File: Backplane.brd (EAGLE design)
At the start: 160 x 84 mm, 2 parts, among them X1 FAC64S

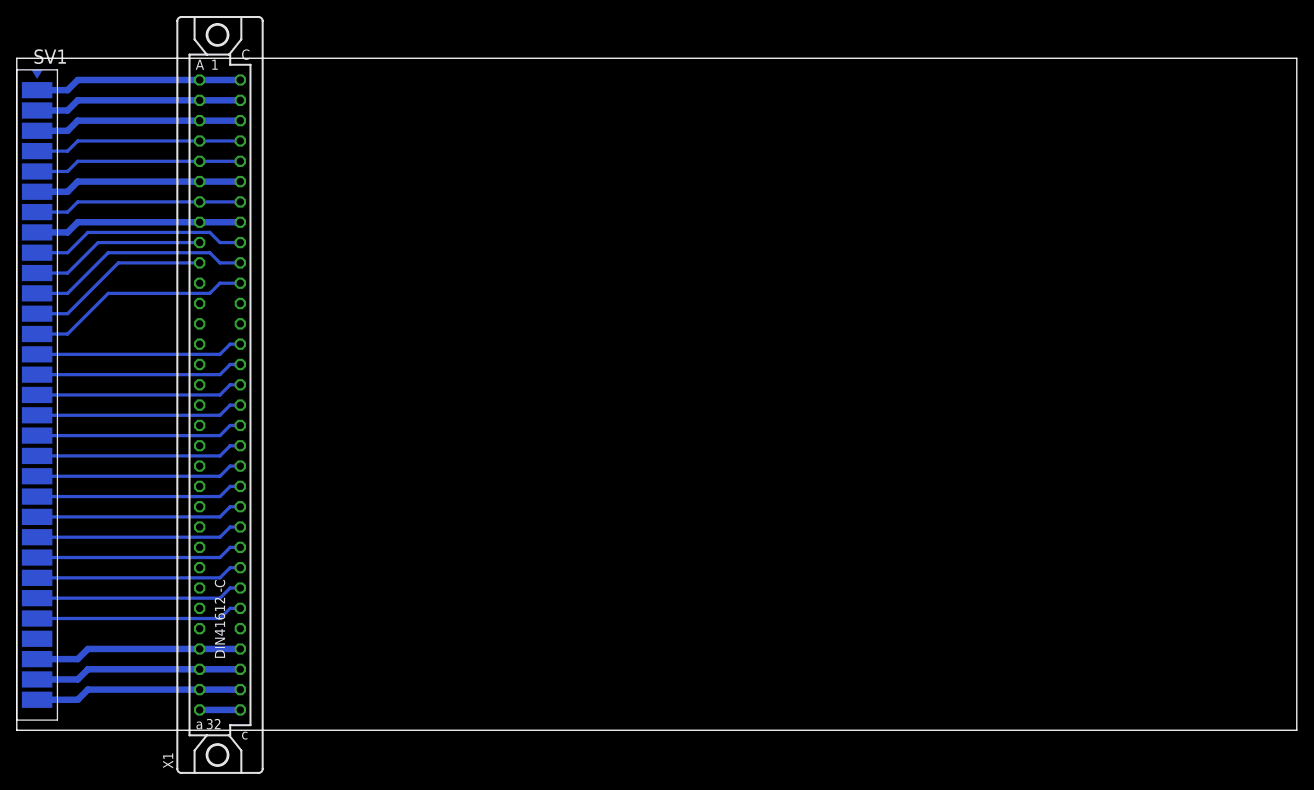
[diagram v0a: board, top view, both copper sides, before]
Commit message: Pi-Display hinzugefügt, Boards angepasst
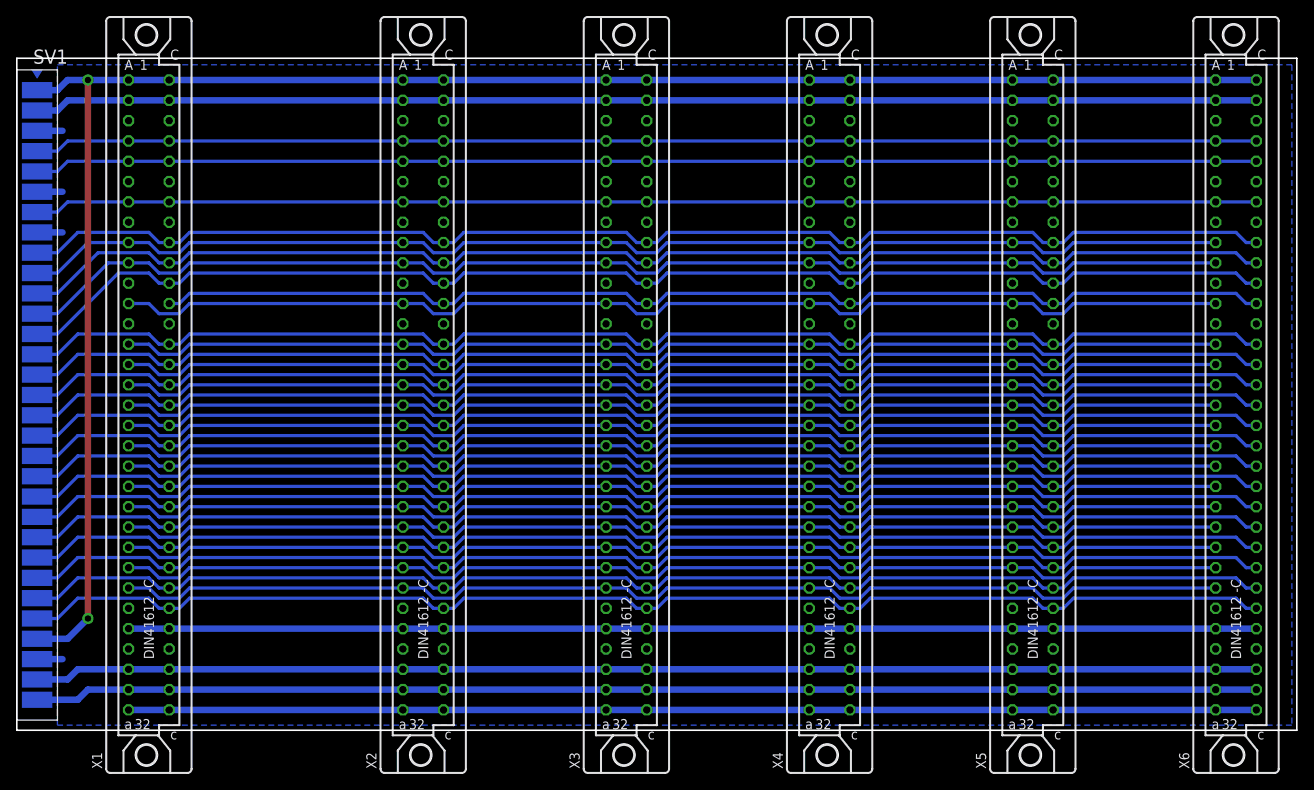
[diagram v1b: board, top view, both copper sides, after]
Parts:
- added X2, X3, X4, X5, X6: FAC64S, con-vg:FAC64S
- moved X1 8.89 mm to (16.5, 41.9)
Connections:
- new net A14: X1.A14, X2.A14, X3.A14, X4.A14, X5.A14, X6.A14
- new net A15: X1.A15, X2.A15, X3.A15, X4.A15, X5.A15, X6.A15
- new net A16: X1.A16, X2.A16, X3.A16, X4.A16, X5.A16, X6.A16
- new net A17: X1.A17, X2.A17, X3.A17, X4.A17, X5.A17, X6.A17
- new net A18: X1.A18, X2.A18, X3.A18, X4.A18, X5.A18, X6.A18
- new net A19: X1.A19, X2.A19, X3.A19, X4.A19, X5.A19, X6.A19
- new net A20: X1.A20, X2.A20, X3.A20, X4.A20, X5.A20, X6.A20
- new net A21: X1.A21, X2.A21, X3.A21, X4.A21, X5.A21, X6.A21
- new net A22: X1.A22, X2.A22, X3.A22, X4.A22, X5.A22, X6.A22
- new net A23: X1.A23, X2.A23, X3.A23, X4.A23, X5.A23, X6.A23
- new net A24: X1.A24, X2.A24, X3.A24, X4.A24, X5.A24, X6.A24
- new net A26: X1.A25, X2.A25, X3.A25, X4.A25, X5.A25, X6.A25
- net !PI_RESET: now also X2.A26, X3.A26, X4.A26, X5.A26, X6.A26
- net +24V: now also X2.A32, X2.C32, X3.A32, X3.C32, X4.A32, X4.C32, X5.A32, X5.C32, X6.A32, X6.C32
- net +3,3V: now also X2.A2, X2.C2, X3.A2, X3.C2, X4.A2, X4.C2, X5.A2, X5.C2, X6.A2, X6.C2
- net +5V_EXT: now also X2.A31, X2.C31, X3.A31, X3.C31, X4.A31, X4.C31, X5.A31, X5.C31, X6.A31, X6.C31
- net +5V_INT: now also X2.A1, X2.C1, X3.A1, X3.C1, X4.A1, X4.C1, X5.A1, X5.C1, X6.A1, X6.C1
- net +5V_INT2: now also X2.A28, X2.C28, X3.A28, X3.C28, X4.A28, X4.C28, X5.A28, X5.C28, X6.A28, X6.C28
- net 1WIRE: now also X2.A7, X2.C7, X3.A7, X3.C7, X4.A7, X4.C7, X5.A7, X5.C7, X6.A7, X6.C7
- net GND: now also X1.A11, X1.A13, X1.A27, X1.C13, X2.A11, X2.A13, X2.A27, X2.A29, X2.A3, X2.A6, X2.A8, X2.C13, X2.C29, X2.C3, X2.C6, X2.C8, X3.A11, X3.A13, X3.A27, X3.A29, X3.A3, X3.A6, X3.A8, X3.C13, X3.C29, X3.C3, X3.C6, X3.C8, X4.A11, X4.A13, X4.A27, X4.A29, X4.A3, X4.A6, X4.A8, X4.C13, X4.C29, X4.C3, X4.C6, X4.C8, X5.A11, X5.A13, X5.A27, X5.A29, X5.A3, X5.A6, X5.A8, X5.C13, X5.C29, X5.C3, X5.C6, X5.C8, X6.A11, X6.A13, X6.A27, X6.A29, X6.A3, X6.A6, X6.A8, X6.C13, X6.C29, X6.C3, X6.C6, X6.C8
- net GND_EXT: now also X2.A30, X2.C30, X3.A30, X3.C30, X4.A30, X4.C30, X5.A30, X5.C30, X6.A30, X6.C30
- net GPIO.05: now also X2.C14, X3.C14, X4.C14, X5.C14, X6.C14
- net GPIO.06: now also X2.C15, X3.C15, X4.C15, X5.C15, X6.C15
- net GPIO.12: now also X2.C16, X3.C16, X4.C16, X5.C16, X6.C16
- net GPIO.13: now also X2.C17, X3.C17, X4.C17, X5.C17, X6.C17
- net GPIO.16: now also X2.C18, X3.C18, X4.C18, X5.C18, X6.C18
- net GPIO.17: now also X2.C19, X3.C19, X4.C19, X5.C19, X6.C19
- net GPIO.18: now also X2.C20, X3.C20, X4.C20, X5.C20, X6.C20
- net GPIO.19: now also X2.C21, X3.C21, X4.C21, X5.C21, X6.C21
- net GPIO.20: now also X2.C22, X3.C22, X4.C22, X5.C22, X6.C22
- net GPIO.21: now also X2.C23, X3.C23, X4.C23, X5.C23, X6.C23
- net GPIO.22: now also X2.C24, X3.C24, X4.C24, X5.C24, X6.C24
- net GPIO.23: now also X2.C25, X3.C25, X4.C25, X5.C25, X6.C25
- net GPIO.24: now also X2.C26, X3.C26, X4.C26, X5.C26, X6.C26
- net GPIO.25: now also X2.C27, X3.C27, X4.C27, X5.C27, X6.C27
- net I2C_SCL: now also X2.A5, X2.C5, X3.A5, X3.C5, X4.A5, X4.C5, X5.A5, X5.C5, X6.A5, X6.C5
- net I2C_SDA: now also X2.A4, X2.C4, X3.A4, X3.C4, X4.A4, X4.C4, X5.A4, X5.C4, X6.A4, X6.C4
- net PI_RXD: now also X2.C12, X3.C12, X4.C12, X5.C12, X6.C12
- net PI_TXD: now also X2.A12, X3.A12, X4.A12, X5.A12, X6.A12
- net SPI_CE0: now also X2.A10, X3.A10, X4.A10, X5.A10, X6.A10
- net SPI_CE1: now also X2.C11, X3.C11, X4.C11, X5.C11, X6.C11
- net SPI_MISO: now also X2.A9, X3.A9, X4.A9, X5.A9, X6.A9
- net SPI_MOSI: now also X2.C9, X3.C9, X4.C9, X5.C9, X6.C9
- net SPI_SCLK: now also X2.C10, X3.C10, X4.C10, X5.C10, X6.C10
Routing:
- net +5V_INT: track 25.9 -> 227.6 mm, vias 0 -> 2
- net A20: track 0.00 -> 141.2 mm
- net A19: track 0.00 -> 141.2 mm
- net A18: track 0.00 -> 141.2 mm
- net A17: track 0.00 -> 141.2 mm
- net A16: track 0.00 -> 141.2 mm
- net PI_TXD: track 0.00 -> 141.2 mm
- net A26: track 0.00 -> 141.2 mm
- net A24: track 0.00 -> 141.2 mm
- net A23: track 0.00 -> 141.2 mm
- net A22: track 0.00 -> 141.2 mm
- net A21: track 0.00 -> 141.2 mm
- net !PI_RESET: track 0.00 -> 141.2 mm
- net PI_RXD: track 0.00 -> 141.2 mm
- net A15: track 0.00 -> 141.2 mm
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- added copper zone on layer 16, net GND
